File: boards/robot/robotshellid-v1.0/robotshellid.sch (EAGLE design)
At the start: 37 parts, among them U1 TCA9548APWR, U2 TCS34725FN, U3 TCS34725FN, U4 TCS34725FN, U5 TCS34725FN, U6 MIC5501-3.0YM5-TR

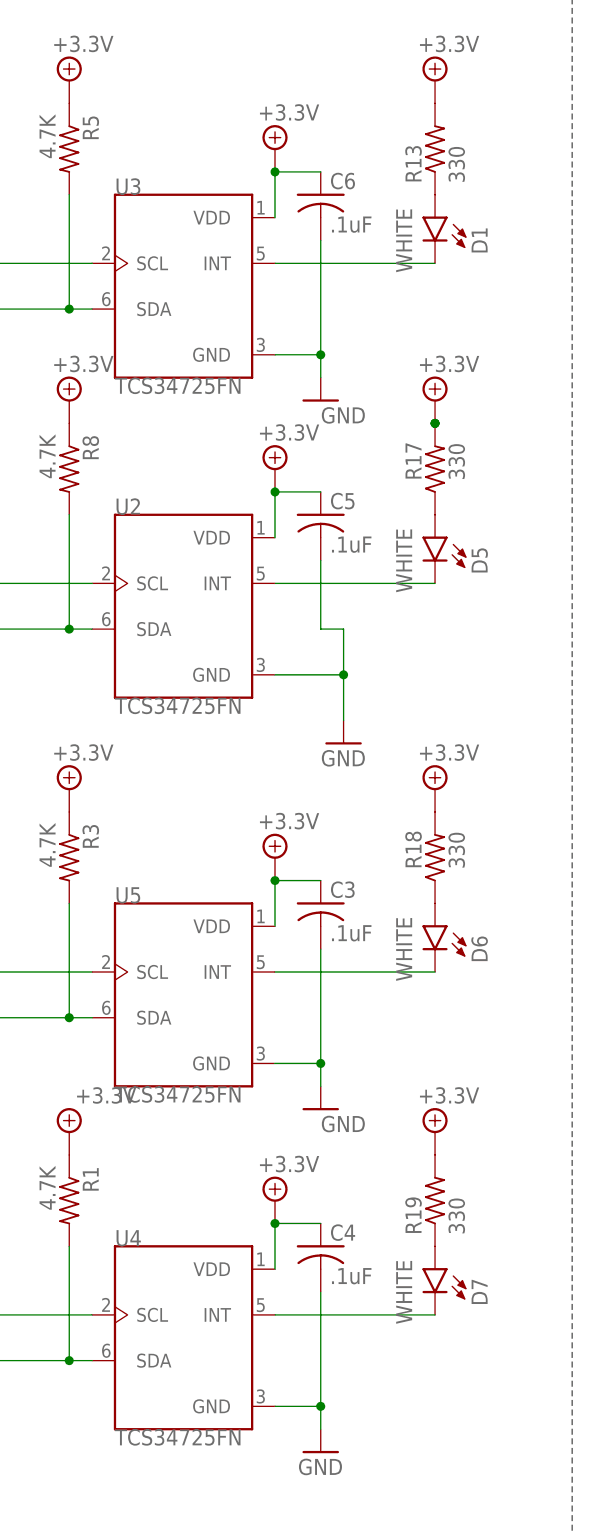
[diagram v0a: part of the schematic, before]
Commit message: Update Silk Screen and trace width
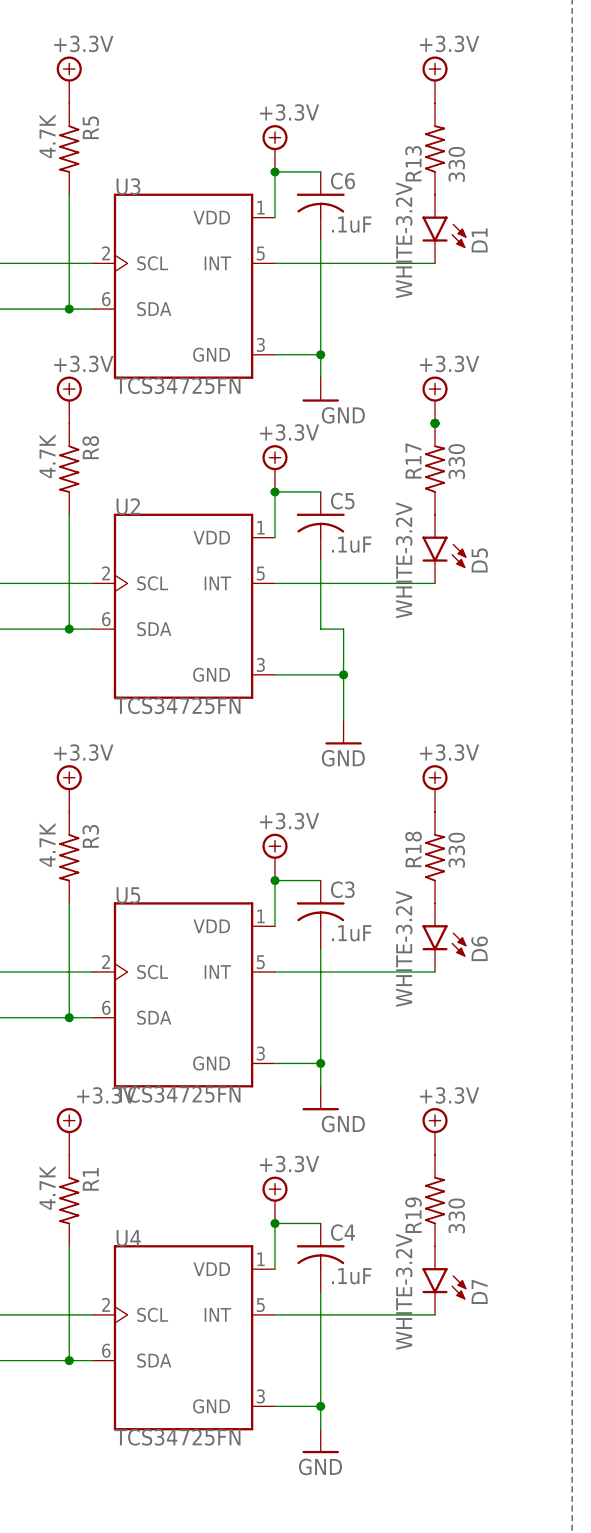
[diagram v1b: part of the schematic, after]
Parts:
- D1, D5, D6, D7: value WHITE -> WHITE-3.2V
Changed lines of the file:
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@@
 <part name="C1" library="rcl" library_urn="urn:adsk.eagle:library:334" deviceset="C-US" device="C0603" package3d_urn="urn:adsk.eagle:package:23616/2" value="1uF"/>
 <part name="C2" library="rcl" library_urn="urn:adsk.eagle:library:334" deviceset="C-US" device="C0603" package3d_urn="urn:adsk.eagle:package:23616/2" value="1uF"/>
-<part name="D1" library="RoboJackets-LEDs" deviceset="LED-SMD" device="" value="WHITE"/>
+<part name="D1" library="RoboJackets-LEDs" deviceset="LED-SMD" device="" value="WHITE-3.2V"/>
 <part name="R13" library="rcl" library_urn="urn:adsk.eagle:library:334" deviceset="R-US_" device="R0603" package3d_urn="urn:adsk.eagle:package:23555/3" value="330"/>
 <part name="SUPPLY28" library="RoboJackets-Supplies" deviceset="+3.3V" device=""/>
-<part name="D5" library="RoboJackets-LEDs" deviceset="LED-SMD" device="" value="WHITE"/>
+<part name="D5" library="RoboJackets-LEDs" deviceset="LED-SMD" device="" value="WHITE-3.2V"/>
 <part name="R17" library="rcl" library_urn="urn:adsk.eagle:library:334" deviceset="R-US_" device="R0603" package3d_urn="urn:adsk.eagle:package:23555/3" value="330"/>
 <part name="SUPPLY32" library="RoboJackets-Supplies" deviceset="+3.3V" device=""/>
-<part name="D6" library="RoboJackets-LEDs" deviceset="LED-SMD" device="" value="WHITE"/>
+<part name="D6" library="RoboJackets-LEDs" deviceset="LED-SMD" device="" value="WHITE-3.2V"/>
 <part name="R18" library="rcl" library_urn="urn:adsk.eagle:library:334" deviceset="R-US_" device="R0603" package3d_urn="urn:adsk.eagle:package:23555/3" value="330"/>
 <part name="SUPPLY33" library="RoboJackets-Supplies" deviceset="+3.3V" device=""/>
-<part name="D7" library="RoboJackets-LEDs" deviceset="LED-SMD" device="" value="WHITE"/>
+<part name="D7" library="RoboJackets-LEDs" deviceset="LED-SMD" device="" value="WHITE-3.2V"/>
 <part name="R19" library="rcl" library_urn="urn:adsk.eagle:library:334" deviceset="R-US_" device="R0603" package3d_urn="urn:adsk.eagle:package:23555/3" value="330"/>
 <part name="SUPPLY34" library="RoboJackets-Supplies" deviceset="+3.3V" device=""/>

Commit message: ASHA notes pt1
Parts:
- D1, D5, D6, D7: value WHITE-3.2V -> WHITE
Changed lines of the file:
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@@
 <part name="C1" library="rcl" library_urn="urn:adsk.eagle:library:334" deviceset="C-US" device="C0603" package3d_urn="urn:adsk.eagle:package:23616/2" value="1uF"/>
 <part name="C2" library="rcl" library_urn="urn:adsk.eagle:library:334" deviceset="C-US" device="C0603" package3d_urn="urn:adsk.eagle:package:23616/2" value="1uF"/>
-<part name="D1" library="RoboJackets-LEDs" deviceset="LED-SMD" device="" value="WHITE-3.2V"/>
+<part name="D1" library="RoboJackets-LEDs" deviceset="LED-SMD" device="" value="WHITE"/>
 <part name="R13" library="rcl" library_urn="urn:adsk.eagle:library:334" deviceset="R-US_" device="R0603" package3d_urn="urn:adsk.eagle:package:23555/3" value="330"/>
 <part name="SUPPLY28" library="RoboJackets-Supplies" deviceset="+3.3V" device=""/>
-<part name="D5" library="RoboJackets-LEDs" deviceset="LED-SMD" device="" value="WHITE-3.2V"/>
+<part name="D5" library="RoboJackets-LEDs" deviceset="LED-SMD" device="" value="WHITE"/>
 <part name="R17" library="rcl" library_urn="urn:adsk.eagle:library:334" deviceset="R-US_" device="R0603" package3d_urn="urn:adsk.eagle:package:23555/3" value="330"/>
 <part name="SUPPLY32" library="RoboJackets-Supplies" deviceset="+3.3V" device=""/>
-<part name="D6" library="RoboJackets-LEDs" deviceset="LED-SMD" device="" value="WHITE-3.2V"/>
+<part name="D6" library="RoboJackets-LEDs" deviceset="LED-SMD" device="" value="WHITE"/>
 <part name="R18" library="rcl" library_urn="urn:adsk.eagle:library:334" deviceset="R-US_" device="R0603" package3d_urn="urn:adsk.eagle:package:23555/3" value="330"/>
 <part name="SUPPLY33" library="RoboJackets-Supplies" deviceset="+3.3V" device=""/>
-<part name="D7" library="RoboJackets-LEDs" deviceset="LED-SMD" device="" value="WHITE-3.2V"/>
+<part name="D7" library="RoboJackets-LEDs" deviceset="LED-SMD" device="" value="WHITE"/>
 <part name="R19" library="rcl" library_urn="urn:adsk.eagle:library:334" deviceset="R-US_" device="R0603" package3d_urn="urn:adsk.eagle:package:23555/3" value="330"/>
 <part name="SUPPLY34" library="RoboJackets-Supplies" deviceset="+3.3V" device=""/>

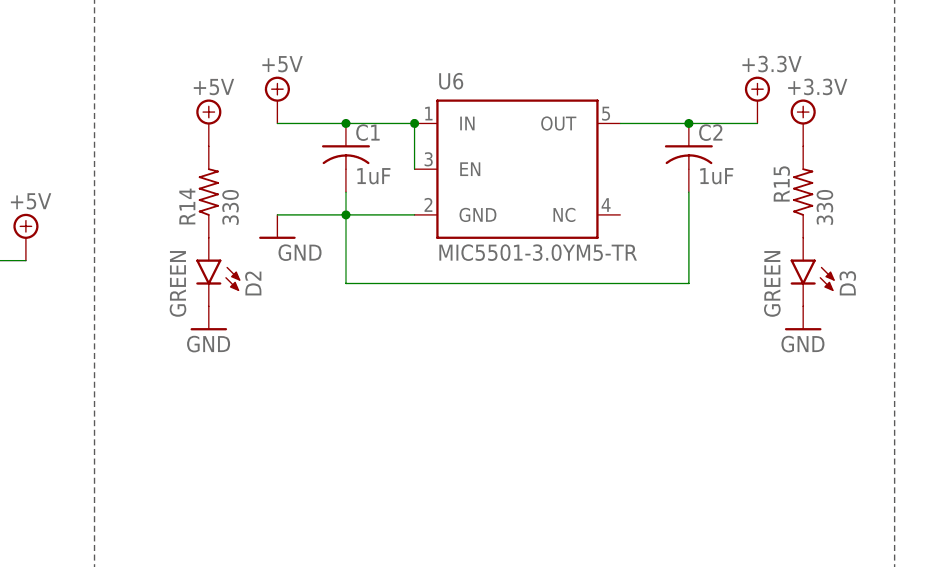
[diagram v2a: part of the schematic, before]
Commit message: Asha notes Pt2
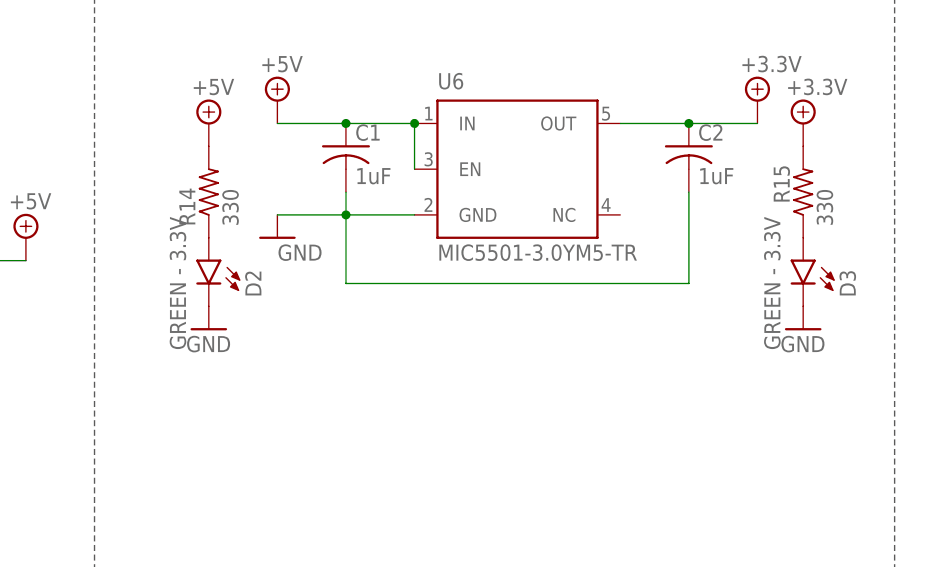
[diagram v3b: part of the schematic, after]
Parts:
- D2, D3: value GREEN -> GREEN - 3.3V
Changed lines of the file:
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@@
 <part name="R19" library="rcl" library_urn="urn:adsk.eagle:library:334" deviceset="R-US_" device="R0603" package3d_urn="urn:adsk.eagle:package:23555/3" value="330"/>
 <part name="SUPPLY34" library="RoboJackets-Supplies" deviceset="+3.3V" device=""/>
-<part name="D2" library="RoboJackets-LEDs" deviceset="LED-SMD" device="" value="GREEN"/>
+<part name="D2" library="RoboJackets-LEDs" deviceset="LED-SMD" device="" value="GREEN - 3.3V"/>
 <part name="R14" library="rcl" library_urn="urn:adsk.eagle:library:334" deviceset="R-US_" device="R0603" package3d_urn="urn:adsk.eagle:package:23555/3" value="330"/>
 <part name="SUPPLY29" library="RoboJackets-Supplies" deviceset="+5V" device=""/>
 <part name="SUPPLY30" library="RoboJackets-Supplies" deviceset="GND" device=""/>
-<part name="D3" library="RoboJackets-LEDs" deviceset="LED-SMD" device="" value="GREEN"/>
+<part name="D3" library="RoboJackets-LEDs" deviceset="LED-SMD" device="" value="GREEN - 3.3V"/>
 <part name="R15" library="rcl" library_urn="urn:adsk.eagle:library:334" deviceset="R-US_" device="R0603" package3d_urn="urn:adsk.eagle:package:23555/3" value="330"/>
 <part name="SUPPLY35" library="RoboJackets-Supplies" deviceset="GND" device=""/>

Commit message: board changes
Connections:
- removed net N$2: D1.C, U3.INT
- removed net N$4: D5.C, U2.INT
- removed net N$6: D6.C, U5.INT
- removed net N$8: D7.C, U4.INT
- net GND: now also D1.C, D5.C, D6.C, D7.C
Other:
- moved on the sheet: D1, D5, D6, D7, R13, R17, R18, R19

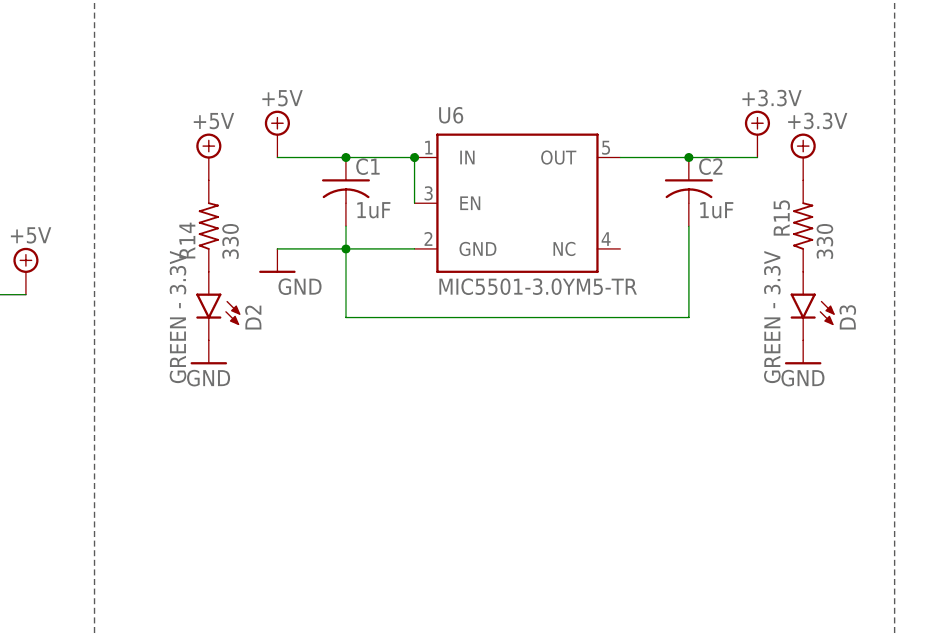
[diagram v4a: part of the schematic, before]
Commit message: Silkscreen stuff
Added some silkscreen components
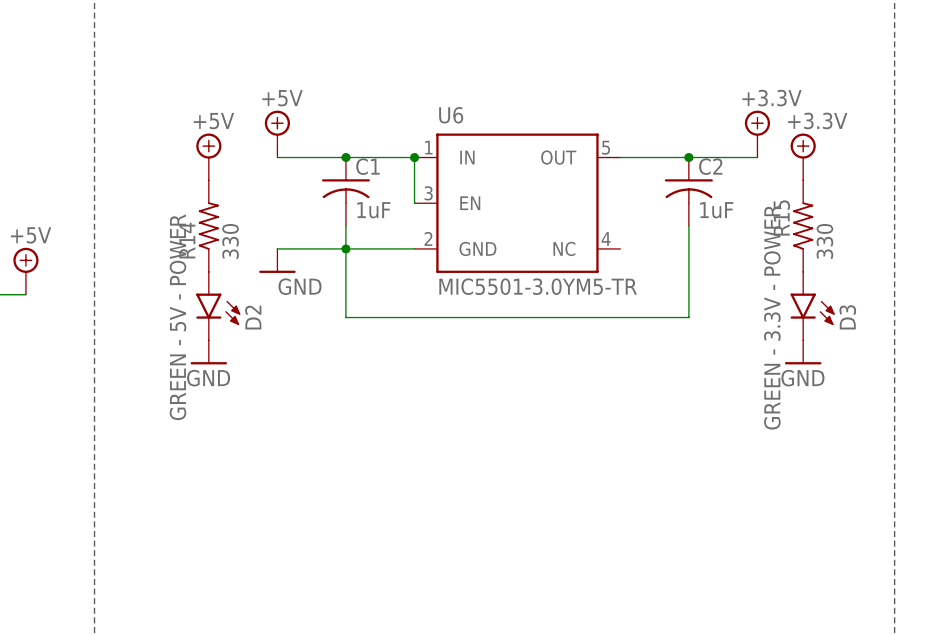
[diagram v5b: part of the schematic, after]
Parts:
- D2: value GREEN - 3.3V -> GREEN - 5V - POWER
- D3: value GREEN - 3.3V -> GREEN - 3.3V - POWER
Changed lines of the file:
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@@
 <part name="R19" library="rcl" library_urn="urn:adsk.eagle:library:334" deviceset="R-US_" device="R0603" package3d_urn="urn:adsk.eagle:package:23555/3" value="330"/>
 <part name="SUPPLY34" library="RoboJackets-Supplies" deviceset="+3.3V" device=""/>
-<part name="D2" library="RoboJackets-LEDs" deviceset="LED-SMD" device="" value="GREEN - 3.3V"/>
+<part name="D2" library="RoboJackets-LEDs" deviceset="LED-SMD" device="" value="GREEN - 5V - POWER"/>
 <part name="R14" library="rcl" library_urn="urn:adsk.eagle:library:334" deviceset="R-US_" device="R0603" package3d_urn="urn:adsk.eagle:package:23555/3" value="330"/>
 <part name="SUPPLY29" library="RoboJackets-Supplies" deviceset="+5V" device=""/>
 <part name="SUPPLY30" library="RoboJackets-Supplies" deviceset="GND" device=""/>
-<part name="D3" library="RoboJackets-LEDs" deviceset="LED-SMD" device="" value="GREEN - 3.3V"/>
+<part name="D3" library="RoboJackets-LEDs" deviceset="LED-SMD" device="" value="GREEN - 3.3V - POWER"/>
 <part name="R15" library="rcl" library_urn="urn:adsk.eagle:library:334" deviceset="R-US_" device="R0603" package3d_urn="urn:adsk.eagle:package:23555/3" value="330"/>
 <part name="SUPPLY35" library="RoboJackets-Supplies" deviceset="GND" device=""/>

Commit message: updated parts
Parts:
- removed U1: TCA9548APWR, robotshellid:TCA9548APWR
- added C7: .1uF, rcl:C-USC0603
- added IC1: PCA9848PWJ, SamacSys_Parts:PCA9848PWJ
- U2, U3, U4, U5: value TCS34725FN -> TSL25721FN; device robotshellid:TCS34725FN -> TSL25721FN:TSL25721FN
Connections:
- removed net A2: JP1.6, U1.A2
- net !RESET: now also IC1.!RESET; no longer U1.!RESET
- net +3.3V: now also C7.1, IC1.VDD1, IC1.VDD2; no longer U1.VCC
- net A0: now also IC1.A0; no longer U1.A0
- net A1: now also IC1.A1; no longer U1.A1
- net GND: now also C7.2, IC1.VSS; no longer U1.GND
- net SCL_CONN: now also IC1.SCL; no longer U1.SCL
- net SCL_SENSOR1: now also IC1.SC4; no longer U1.SC4
- net SCL_SENSOR2: now also IC1.SC5; no longer U1.SC5
- net SCL_SENSOR3: now also IC1.SC6; no longer U1.SC6
- net SCL_SENSOR4: now also IC1.SC7; no longer U1.SC7
- net SDA_CONN: now also IC1.SDA; no longer U1.SDA
- net SDA_SENSOR1: now also IC1.SD4; no longer U1.SD4
- net SDA_SENSOR2: now also IC1.SD5; no longer U1.SD5
- net SDA_SENSOR3: now also IC1.SD6; no longer U1.SD6
- net SDA_SENSOR4: now also IC1.SD7; no longer U1.SD7
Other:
- moved on the sheet: C3, C4, C5, C6, C8, R1, R11, R12, R3, R5, R8, R9
